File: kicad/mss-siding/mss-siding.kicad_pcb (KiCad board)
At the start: 2 copper layers, 127 x 76.2 mm, 147 parts, among them J1 Molex 0532610471, J10 Screw_Terminal_01x02, J11 Molex 0532610471, J12 Molex 0532610471, J13 8P8C, J14 SM04B-SRSS, J15 SM04B-SRSS, J16 SM04B-SRSS, J17 SM04B-SRSS, J18 AVR-ISP, J19 Screw_Terminal_01x02, J2 Molex 0532610471, J3 Screw_Terminal_01x02, J4 8P8C, J5 Screw_Terminal_01x02, J6 Screw_Terminal_01x02, J7 Screw_Terminal_01x02, J8 8P8C, J9 Screw_Terminal_01x02, K1 AGQ200A4H, K2 AGQ200A4H, K3 AGQ200A4H, Q1 ZXMS6004FF, Q2 DRDC3105-7, SW1 JS202011SCQN, SW2 JS202011SCQN, U1 AP63205WU, U2 AP3012, U3 74HC4049, U4 74HC4049, U5 PCA9555PW, U6 ATtiny861A-S, U7 WS2812B

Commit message: Fix a couple more booboos
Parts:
- moved J19 7.01 mm to (102.8, 124.3), turned to 180 degrees
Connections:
- J19 pad 1: GND -> +5V
- J19 pad 3: +5V -> GND
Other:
- board text added: "TURNOUT DIVERGING POS=GND"
- board text removed: "DIVERGING POS=GND"

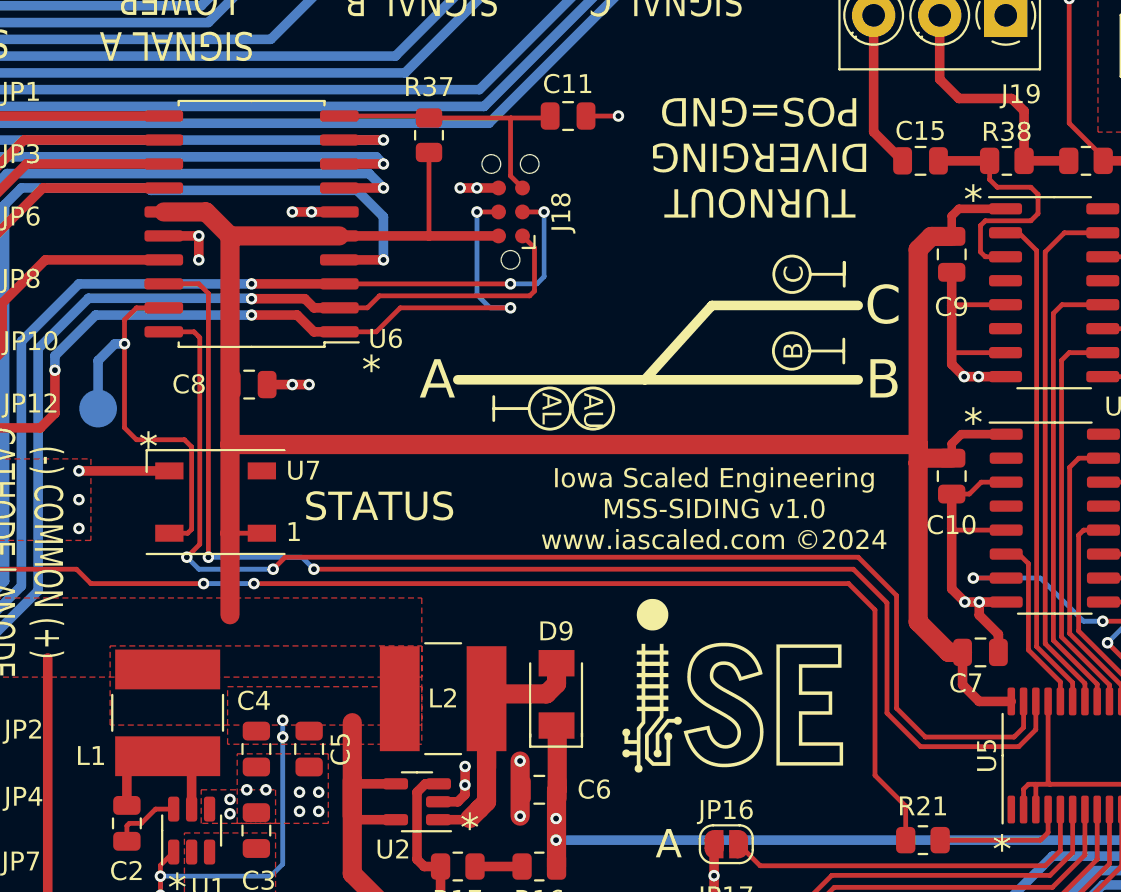
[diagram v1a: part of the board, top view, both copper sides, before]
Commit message: Add I2C pull up resistors Fix some text issues
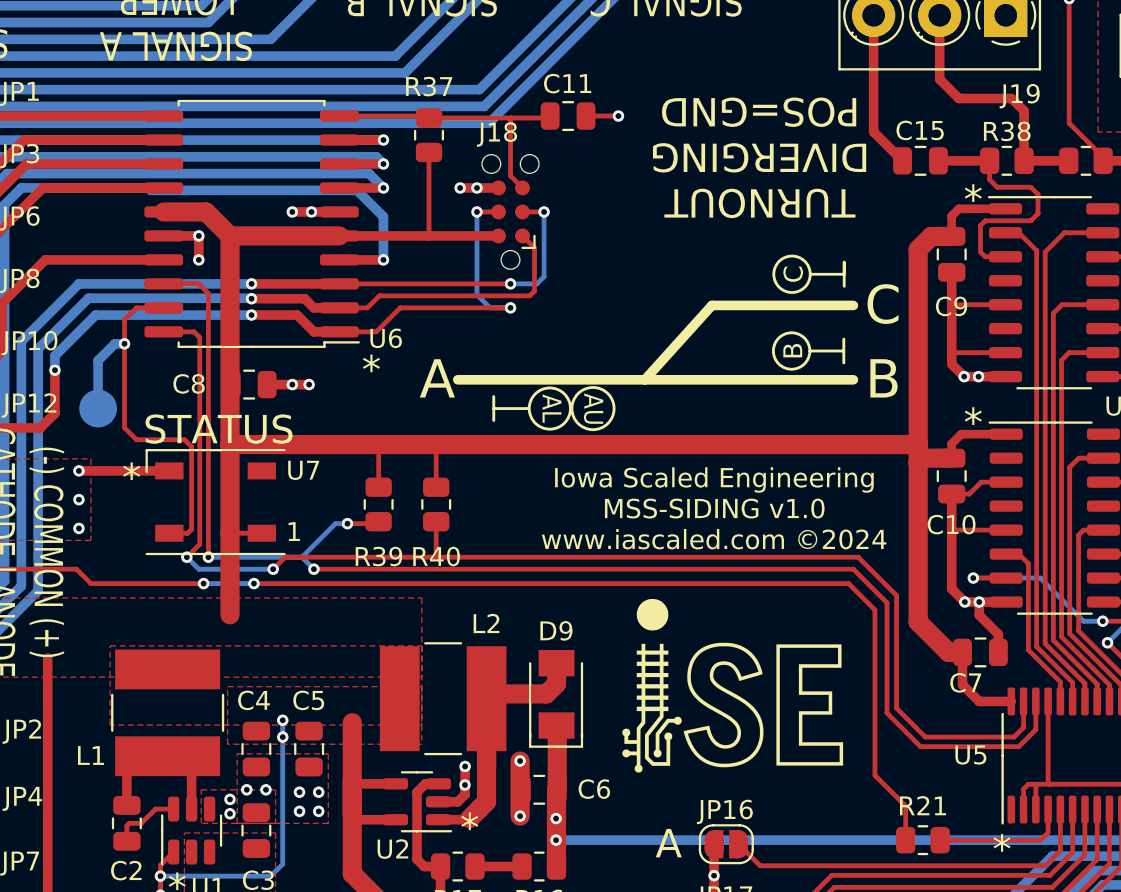
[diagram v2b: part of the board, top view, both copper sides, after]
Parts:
- added R39: 10k, Resistor_SMD:R_0805_2012Metric, F.Cu at (69.6, 150.2)
- added R40: 10k, Resistor_SMD:R_0805_2012Metric, F.Cu at (72.6, 150.2)
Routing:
- net Net-(U5-Pad22): track 69.8 -> 74.7 mm, vias 2 -> 3
- net +5V: track 434.0 -> 438.6 mm
- net Net-(U5-Pad23): track 67.8 -> 69.7 mm

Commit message: Design review improvements
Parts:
- added JP21: SolderJumper_2_Bridged, Jumper:SolderJumper-2_P1.3mm_Bridged_RoundedPad1.0x1.5mm, B.Cu at (109.1, 132.1)
- JP14, JP15, JP5: moved to B.Cu
- moved TP15 51.3 mm to (82.7, 165.4)
- moved R29 15.8 mm to (122.7, 134.1)
- moved R2 3.26 mm to (122.7, 130.8)
- moved JP5 2.48 mm to (117.0, 177.0)
- moved JP14 2.37 mm to (142.2, 176.9)
- moved JP15 2.16 mm to (124.1, 130.3)
- moved R39 1.78 mm to (67.8, 150.2)
- moved R40 1.78 mm to (70.9, 150.2)
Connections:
- R29 pad 2: /TO_NORMAL -> Net-(R29-Pad2)
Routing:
- net +12V: track 122.7 -> 99.4 mm, vias 8 -> 7
- net GND: track 166.7 -> 144.5 mm
- net Net-(R29-Pad2): track 0.00 -> 14.2 mm, vias 0 -> 2
- net Net-(R1-Pad1): track 3.30 -> 9.17 mm
- net /TO_NORMAL: track 18.1 -> 21.6 mm, vias 0 -> 2
- net Net-(J4-Pad7): track 7.35 -> 4.52 mm
- net Net-(J8-Pad7): track 7.42 -> 4.93 mm
- net Net-(J13-Pad7): track 7.45 -> 5.29 mm
- net +5V: track 438.6 -> 440.8 mm
- net Net-(R2-Pad1): track 8.49 -> 6.63 mm
- net Net-(J10-Pad2): track 122.1 -> 123.7 mm
- net /A_L_SIGNAL_Y: track 22.6 -> 21.1 mm
- net Net-(R39-Pad1): track 74.7 -> 73.5 mm
- net Net-(J10-Pad1): track 111.4 -> 112.5 mm
- net /B_SIGNAL_R: track 66.0 -> 67.0 mm
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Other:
- board text added: "Cut JP14 to disconnect MSS Port B Pin 7 from ground"
- board text added: "Cut JP15 to disconnect MSS Port A Pin 7 from ground"
- board text added: "Cut JP21 to disable +12V pull-up on turnout IN line"
- board text added: "Cut JP5 to disconnect MSS Port C Pin 7 from ground"
- board text added: "IN"
- board text added: "MSS"
- board text added: "MSS-SIDING v1.0 www.iascaled.com ©2024 Iowa Scaled Engineering"
- board text added: "TURNOUT DIVERGING IN=GND"
- board text removed: "Iowa Scaled Engineering MSS-SIDING v1.0 www.iascaled.com ©2024"
- board text removed: "POS"
- board text removed: "TURNOUT DIVERGING POS=GND"

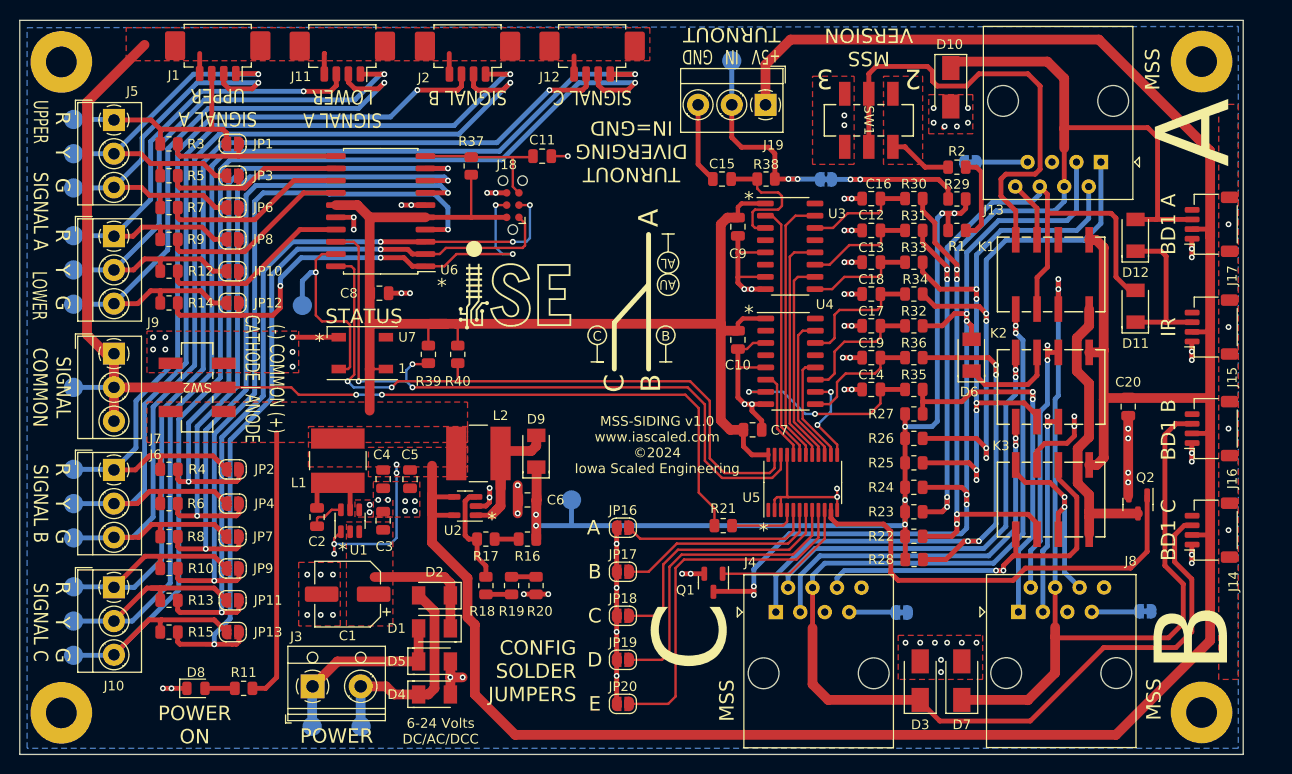
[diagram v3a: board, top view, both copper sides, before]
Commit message: Work on v1.1 that adds the lines needed for approach lighting on the frog end.
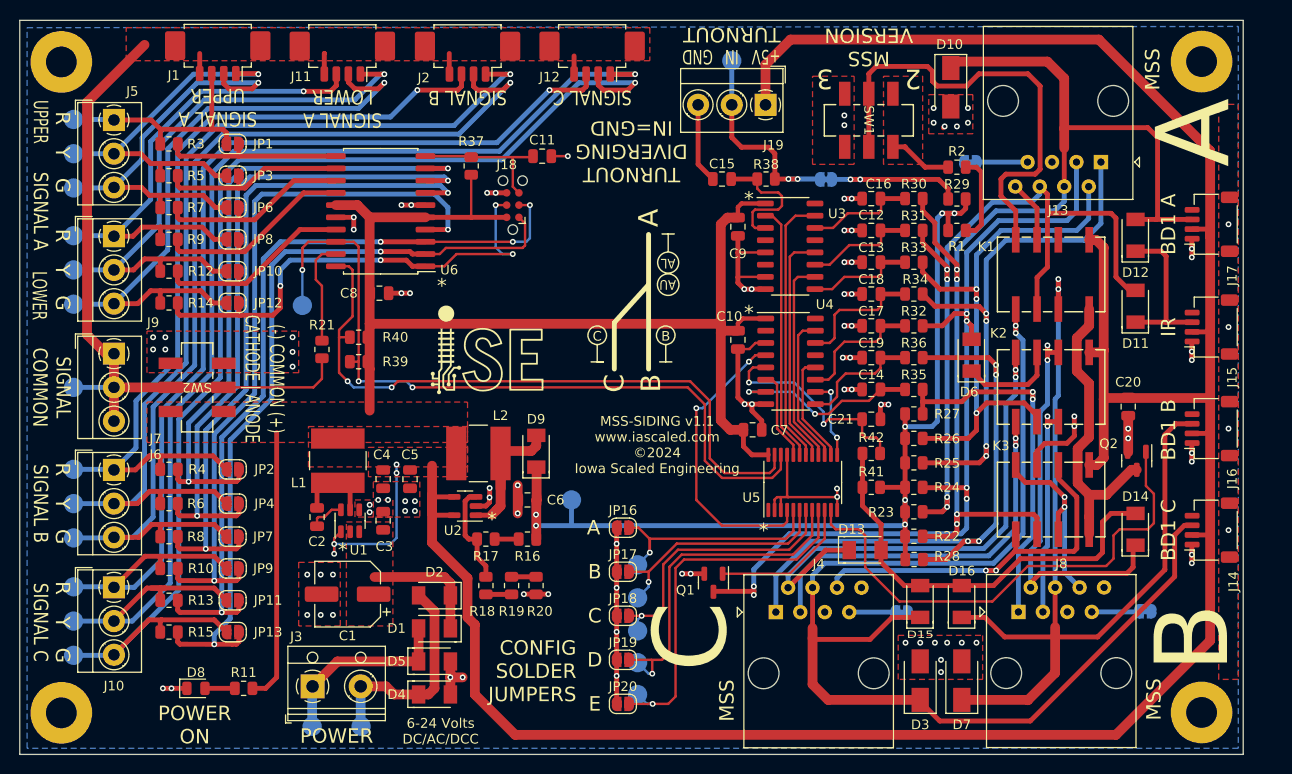
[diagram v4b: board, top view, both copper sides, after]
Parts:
- removed U7: WS2812B, LED_SMD:LED_WS2812B_PLCC4_5.0x5.0mm_P3.2mm
- added C21: 0.1uF, Capacitor_SMD:C_0805_2012Metric, F.Cu at (113.8, 157.0)
- added D13: CDBM140G, ISE_Generic:SOD-123T, F.Cu at (113.2, 170.6)
- added D14: CDBM140G, ISE_Generic:SOD-123T, F.Cu at (141.2, 168.4)
- added D15: CDBM140G, ISE_Generic:SOD-123T, F.Cu at (118.9, 175.9)
- added D16: CDBM140G, ISE_Generic:SOD-123T, F.Cu at (123.2, 175.9)
- added R41: 10k, Resistor_SMD:R_0805_2012Metric, F.Cu at (113.8, 164.0)
- added R42: 10k, Resistor_SMD:R_0805_2012Metric, F.Cu at (113.8, 160.5)
- added TP19: TestPoint, TestPoint:TestPoint_Pad_D2.0mm, B.Cu at (89.5, 172.1)
- added TP20: TestPoint, TestPoint:TestPoint_Pad_D2.0mm, B.Cu at (89.5, 175.5)
- added TP21: TestPoint, TestPoint:TestPoint_Pad_D2.0mm, B.Cu at (89.5, 178.9)
- added TP22: TestPoint, TestPoint:TestPoint_Pad_D2.0mm, B.Cu at (89.5, 182.2)
- added TP23: TestPoint, TestPoint:TestPoint_Pad_D2.0mm, B.Cu at (89.5, 185.5)
- moved R21 45.5 mm to (56.8, 149.7), turned to -90 degrees
- moved R40 10.4 mm to (60.6, 148.5), turned to 0 degrees
- moved R39 7.28 mm to (60.6, 151.0), turned to 0 degrees
- moved Q2 4.53 mm to (141.4, 161.3)
- turned R25 to 0 degrees
- turned R26 to 180 degrees
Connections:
- R25 pad 1: /POINTS_A_IN -> +12V
- R25 pad 2: +12V -> /POINTS_AA_IN
- R26 pad 1: +12V -> /POINTS_A_IN
- R26 pad 2: /POINTS_AA_IN -> +12V
- TP17 pad 1: Net-(TP17-Pad1) -> Net-(R39-Pad1)
- U4 pad 4: unconnected-(U4-Pad4) -> /APPR_LT
- U4 pad 5: GND -> Net-(C21-Pad1)
- U5 pad 4: /COM_SENSE -> /APPR_LT
- U6 pad 19: Net-(TP17-Pad1) -> /COM_SENSE
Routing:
- net Net-(J1-Pad4): track 130.0 -> 79.7 mm, vias 2 -> 0
- net Net-(D13-Pad2): track 0.00 -> 44.2 mm
- net /APPR_LT: track 0.00 -> 30.9 mm, vias 0 -> 2
- net Net-(C21-Pad1): track 0.00 -> 22.6 mm, vias 0 -> 2
- net Net-(TP17-Pad1): track 22.0 -> 0.00 mm, vias 1 -> 0
- net /MAIN_A_IN: track 28.5 -> 42.6 mm
- net GND: track 144.5 -> 134.6 mm
- net +5V: track 440.8 -> 432.7 mm
- net /SIDE_A_IN: track 45.2 -> 53.2 mm
- net Net-(R39-Pad1): track 73.5 -> 80.4 mm
- net /RELAY_DRV: track 45.9 -> 52.8 mm
- net /POINTS_A_IN: track 63.4 -> 56.9 mm, vias 6 -> 3
- net /SIDE_S: track 117.2 -> 123.5 mm
- net /OPTION_A: track 20.0 -> 24.7 mm, vias 0 -> 1
- net /MAIN_S: track 92.2 -> 96.7 mm
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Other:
- board text added: "MSS-SIDING v1.1 www.iascaled.com ©2024 Iowa Scaled Engineering"
- board text removed: "MSS-SIDING v1.0 www.iascaled.com ©2024 Iowa Scaled Engineering"
- board text removed: "STATUS"
